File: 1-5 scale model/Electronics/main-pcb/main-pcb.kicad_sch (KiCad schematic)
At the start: 21 parts

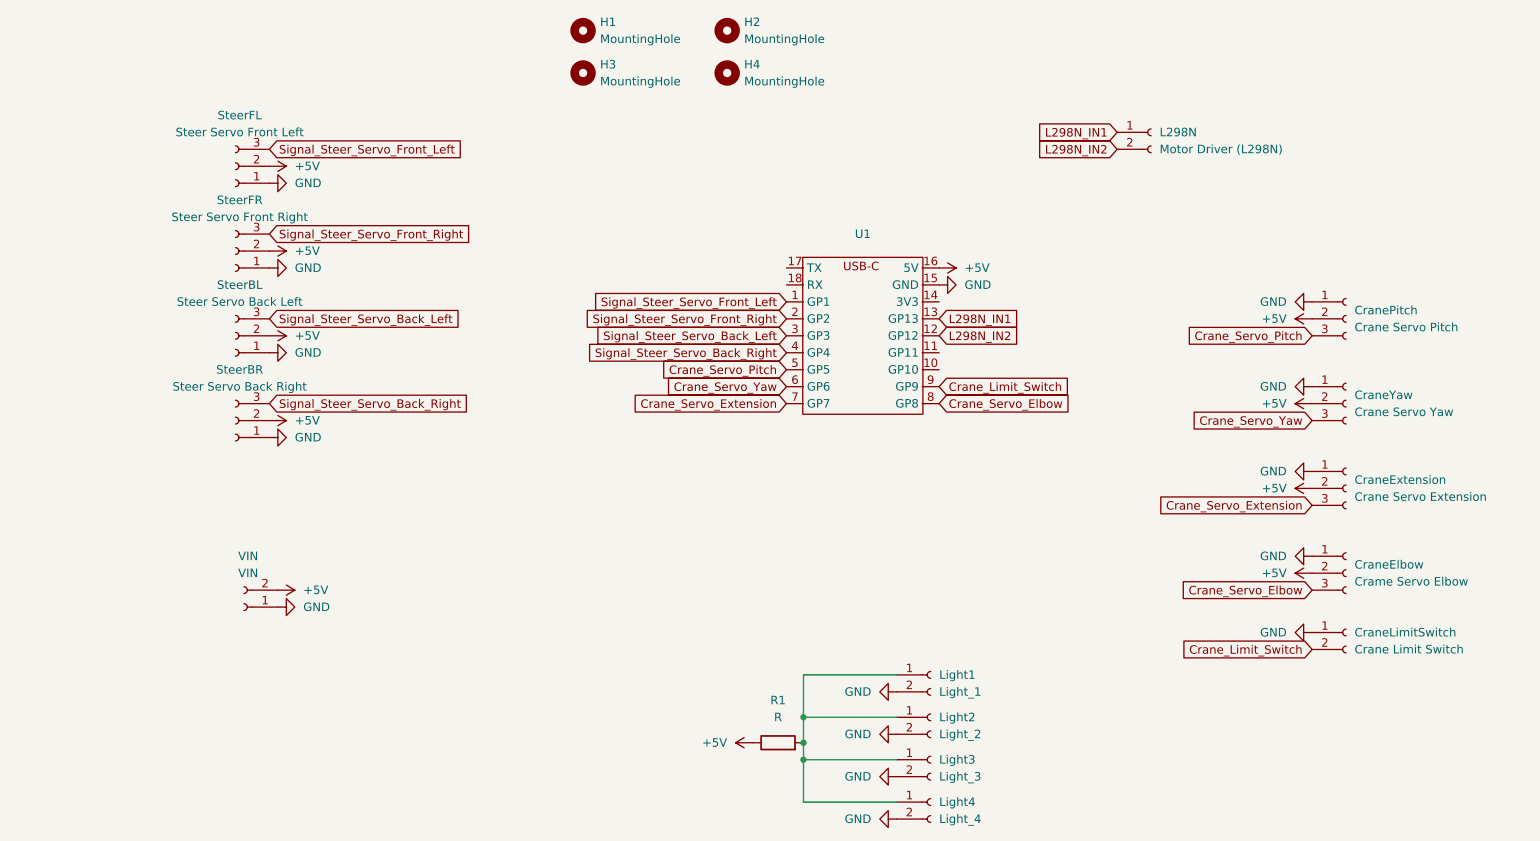
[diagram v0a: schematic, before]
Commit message: updated pitch motor
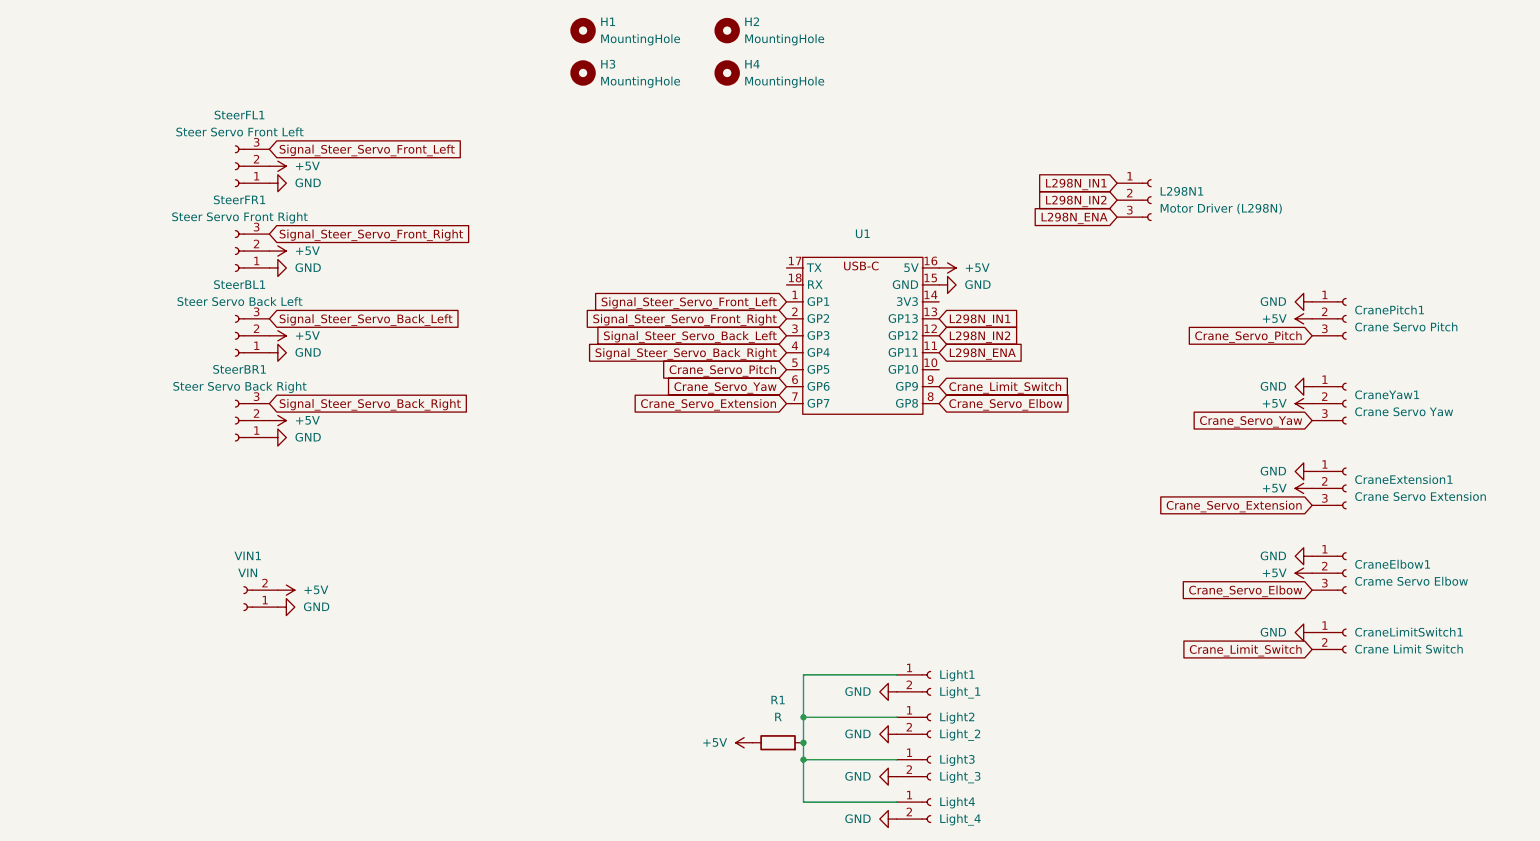
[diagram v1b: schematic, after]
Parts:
- removed L298N: Motor Driver (L298N), Connector_JST:JST_XH_B2B-XH-A_1x02_P2.50mm_Vertical, symbol Connector:Conn_01x02_Socket
- added L298N1: Motor Driver (L298N), Connector_JST:JST_XH_B3B-XH-A_1x03_P2.50mm_Vertical, symbol Connector:Conn_01x03_Socket
- renumbered CraneElbow to CraneElbow1, CraneExtension to CraneExtension1, CraneLimitSwitch to CraneLimitSwitch1, CranePitch to CranePitch1, CraneYaw to CraneYaw1, SteerBL to SteerBL1, SteerBR to SteerBR1, SteerFL to SteerFL1, SteerFR to SteerFR1, VIN to VIN1
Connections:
- net L298N_IN1: now also L298N1.1 (Pin_1)
- net L298N_IN2: now also L298N1.2 (Pin_2)
- net L298N_ENA: now reaches U1.11 (GP11)
- net L298N_ENA: now also L298N1.3 (Pin_3)
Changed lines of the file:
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@@
 		)
 	)
-	(global_label "L298N_IN1"
-		(shape input)
-		(at 195.58 53.34 180)
-		(fields_autoplaced yes)
-		(effects
-			(font
-				(size 1.27 1.27)
-			)
-			(justify right)
-		)
-		(property "Intersheetrefs" "${INTERSHEET_REFS}"
-			(at 182.4953 53.34 0)
-			(effects
-				(font
-					(size 1.27 1.27)
-				)
-				(justify right)
-				(hide yes)
-			)
-		)
-	)
 	(global_label "Signal_Steer_Servo_Back_Left"
 		(shape input)
@@
 		)
 	)
+	(global_label "L298N_IN2"
+		(shape input)
+		(at 195.58 63.5 180)
+		(fields_autoplaced yes)
+		(effects
+			(font
+				(size 1.27 1.27)
+			)
+			(justify right)
+		)
+		(property "Intersheetrefs" "${INTERSHEET_REFS}"
+			(at 182.4953 63.5 0)
+			(effects
+				(font
+					(size 1.27 1.27)
+				)
+				(justify right)
+				(hide yes)
+			)
+		)
+	)
 	(global_label "Signal_Steer_Servo_Back_Right"
 		(shape input)
@@
 		)
 	)
-	(global_label "L298N_IN2"
+	(global_label "Signal_Steer_Servo_Back_Left"
 		(shape input)
-		(at 195.58 55.88 180)
+		(at 68.58 81.28 0)
 		(fields_autoplaced yes)
 		(effects
@@
 				(size 1.27 1.27)
 			)
-			(justify right)
+			(justify left)
 		)
 		(property "Intersheetrefs" "${INTERSHEET_REFS}"
-			(at 182.4953 55.88 0)
+			(at 99.5654 81.28 0)
 			(effects
 				(font
 					(size 1.27 1.27)
 				)
-				(justify right)
+				(justify left)
 				(hide yes)
 			)
 		)
 	)
-	(global_label "Signal_Steer_Servo_Back_Left"
+	(global_label "Crane_Servo_Elbow"
 		(shape input)
-		(at 68.58 81.28 0)
+		(at 168.91 93.98 0)
 		(fields_autoplaced yes)
 		(effects
@@
 		)
 		(property "Intersheetrefs" "${INTERSHEET_REFS}"
-			(at 99.5654 81.28 0)
+			(at 189.9168 93.98 0)
 			(effects
 				(font
@@
 		)
 	)
-	(global_label "Crane_Servo_Elbow"
+	(global_label "Crane_Servo_Extension"
 		(shape input)
-		(at 168.91 93.98 0)
+		(at 146.05 93.98 180)
+		(fields_autoplaced yes)
+		(effects
+			(font
+				(size 1.27 1.27)
+			)
+			(justify right)
+		)
+		(property "Intersheetrefs" "${INTERSHEET_REFS}"
+			(at 121.4146 93.98 0)
+			(effects
+				(font
+					(size 1.27 1.27)
+				)
+				(justify right)
+				(hide yes)
+			)
+		)
+	)
+	(global_label "L298N_ENA"
+		(shape input)
+		(at 168.91 86.36 0)
 		(fields_autoplaced yes)
 		(effects
@@
 		)
 		(property "Intersheetrefs" "${INTERSHEET_REFS}"
-			(at 189.9168 93.98 0)
+			(at 182.418 86.36 0)
 			(effects
 				(font
@@
 		)
 	)
-	(global_label "Crane_Servo_Extension"
+	(global_label "L298N_IN1"
 		(shape input)
-		(at 146.05 93.98 180)
+		(at 195.58 60.96 180)
 		(fields_autoplaced yes)
 		(effects
@@
 		)
 		(property "Intersheetrefs" "${INTERSHEET_REFS}"
-			(at 121.4146 93.98 0)
+			(at 182.4953 60.96 0)
 			(effects
 				(font
@@
 		)
 	)
+	(global_label "L298N_ENA"
+		(shape input)
+		(at 195.58 66.04 180)
+		(fields_autoplaced yes)
+		(effects
+			(font
+				(size 1.27 1.27)
+			)
+			(justify right)
+		)
+		(property "Intersheetrefs" "${INTERSHEET_REFS}"
+			(at 182.072 66.04 0)
+			(effects
+				(font
+					(size 1.27 1.27)
+				)
+				(justify right)
+				(hide yes)
+			)
+		)
+	)
 	(symbol
 		(lib_id "power:+5V")
@@
 		(dnp no)
 		(fields_autoplaced yes)
-		(property "Reference" "CraneExtension"
+		(property "Reference" "CraneExtension1"
 			(at 231.14 105.4099 0)
 			(effects
@@
 			(project "main-pcb"
 				(path "/7ea8da9e-64ae-49f9-b37e-5eaa0e3ec503"
-					(reference "CraneExtension")
+					(reference "CraneExtension1")
 					(unit 1)
 				)
@@
 	)
 	(symbol
+		(lib_id "Connector:Conn_01x03_Socket")
+		(at 200.66 63.5 0)
+		(unit 1)
+		(exclude_from_sim no)
+		(in_bom yes)
+		(on_board yes)
+		(dnp no)
+		(fields_autoplaced yes)
+		(property "Reference" "L298N1"
+			(at 201.93 62.2299 0)
+			(effects
+				(font
+					(size 1.27 1.27)
+				)
+				(justify left)
+			)
+		)
+		(property "Value" "Motor Driver (L298N)"
+			(at 201.93 64.7699 0)
+			(effects
+				(font
+					(size 1.27 1.27)
+				)
+				(justify left)
+			)
+		)
+		(property "Footprint" "Connector_JST:JST_XH_B3B-XH-A_1x03_P2.50mm_Vertical"
+			(at 200.66 63.5 0)
+			(effects
+				(font
+					(size 1.27 1.27)
+				)
+				(hide yes)
+			)
+		)
+		(property "Datasheet" "~"
+			(at 200.66 63.5 0)
+			(effects
+				(font
+					(size 1.27 1.27)
+				)
+				(hide yes)
+			)
+		)
+		(property "Description" "Generic connector, single row, 01x03, script generated"
+			(at 200.66 63.5 0)
+			(effects
+				(font
+					(size 1.27 1.27)
+				)
+				(hide yes)
+			)
+		)
+		(pin "2"
+		)
+		(pin "1"
+		)
+		(pin "3"
+		)
+		(instances
+			(project "main-pcb"
+				(path "/7ea8da9e-64ae-49f9-b37e-5eaa0e3ec503"
+					(reference "L298N1")
+					(unit 1)
+				)
+			)
+		)
+	)
+	(symbol
 		(lib_id "Connector:Conn_01x02_Socket")
 		(at 64.77 124.46 180)
@@
 		(dnp no)
 		(fields_autoplaced yes)
-		(property "Reference" "VIN"
+		(property "Reference" "VIN1"
 			(at 65.405 116.84 0)
 			(effects
@@
 			(project "main-pcb"
 				(path "/7ea8da9e-64ae-49f9-b37e-5eaa0e3ec503"
-					(reference "VIN")
+					(reference "VIN1")
 					(unit 1)
 				)
@@
 		(dnp no)
 		(fields_autoplaced yes)
-		(property "Reference" "SteerBL"
+		(property "Reference" "SteerBL1"
 			(at 64.135 76.2 0)
 			(effects
@@
 			(project "main-pcb"
 				(path "/7ea8da9e-64ae-49f9-b37e-5eaa0e3ec503"
-					(reference "SteerBL")
+					(reference "SteerBL1")
 					(unit 1)
 				)
@@
 		(dnp no)
 		(fields_autoplaced yes)
-		(property "Reference" "SteerFR"
+		(property "Reference" "SteerFR1"
 			(at 64.135 63.5 0)
 			(effects
@@
 			(project "main-pcb"
 				(path "/7ea8da9e-64ae-49f9-b37e-5eaa0e3ec503"
-					(reference "SteerFR")
-					(unit 1)
-				)
-			)
-		)
-	)
-	(symbol
-		(lib_id "Connector:Conn_01x02_Socket")
-		(at 200.66 53.34 0)
-		(unit 1)
-		(exclude_from_sim no)
-		(in_bom yes)
-		(on_board yes)
-		(dnp no)
-		(fields_autoplaced yes)
-		(property "Reference" "L298N"
-			(at 201.93 53.3399 0)
-			(effects
-				(font
-					(size 1.27 1.27)
-				)
-				(justify left)
-			)
-		)
-		(property "Value" "Motor Driver (L298N)"
-			(at 201.93 55.8799 0)
-			(effects
-				(font
-					(size 1.27 1.27)
-				)
-				(justify left)
-			)
-		)
-		(property "Footprint" "Connector_JST:JST_XH_B2B-XH-A_1x02_P2.50mm_Vertical"
-			(at 200.66 53.34 0)
-			(effects
-				(font
-					(size 1.27 1.27)
-				)
-				(hide yes)
-			)
-		)
-		(property "Datasheet" "~"
-			(at 200.66 53.34 0)
-			(effects
-				(font
-					(size 1.27 1.27)
-				)
-				(hide yes)
-			)
-		)
-		(property "Description" "Generic connector, single row, 01x02, script generated"
-			(at 200.66 53.34 0)
-			(effects
-				(font
-					(size 1.27 1.27)
-				)
-				(hide yes)
-			)
-		)
-		(pin "1"
-		)
-		(pin "2"
-		)
-		(instances
-			(project "main-pcb"
-				(path "/7ea8da9e-64ae-49f9-b37e-5eaa0e3ec503"
-					(reference "L298N")
+					(reference "SteerFR1")
 					(unit 1)
 				)
@@
 		(dnp no)
 		(fields_autoplaced yes)
-		(property "Reference" "SteerBR"
+		(property "Reference" "SteerBR1"
 			(at 64.135 88.9 0)
 			(effects
@@
 			(project "main-pcb"
 				(path "/7ea8da9e-64ae-49f9-b37e-5eaa0e3ec503"
-					(reference "SteerBR")
+					(reference "SteerBR1")
 					(unit 1)
 				)
@@
 		(dnp no)
 		(fields_autoplaced yes)
-		(property "Reference" "CraneLimitSwitch"
+		(property "Reference" "CraneLimitSwitch1"
 			(at 231.14 128.2699 0)
 			(effects
@@
 			(project ""
 				(path "/7ea8da9e-64ae-49f9-b37e-5eaa0e3ec503"
-					(reference "CraneLimitSwitch")
+					(reference "CraneLimitSwitch1")
 					(unit 1)
 				)
@@
 		(dnp no)
 		(fields_autoplaced yes)
-		(property "Reference" "CraneElbow"
+		(property "Reference" "CraneElbow1"
 			(at 231.14 118.1099 0)
 			(effects
@@
 			(project "main-pcb"
 				(path "/7ea8da9e-64ae-49f9-b37e-5eaa0e3ec503"
-					(reference "CraneElbow")
+					(reference "CraneElbow1")
 					(unit 1)
 				)
@@
 		(dnp no)
 		(fields_autoplaced yes)
-		(property "Reference" "SteerFL"
+		(property "Reference" "SteerFL1"
 			(at 64.135 50.8 0)
 			(effects
@@
 			(project "main-pcb"
 				(path "/7ea8da9e-64ae-49f9-b37e-5eaa0e3ec503"
-					(reference "SteerFL")
+					(reference "SteerFL1")
 					(unit 1)
 				)
@@
 		(dnp no)
 		(fields_autoplaced yes)
-		(property "Reference" "CraneYaw"
+		(property "Reference" "CraneYaw1"
 			(at 231.14 92.7099 0)
 			(effects
@@
 			(project "main-pcb"
 				(path "/7ea8da9e-64ae-49f9-b37e-5eaa0e3ec503"
-					(reference "CraneYaw")
+					(reference "CraneYaw1")
 					(unit 1)
 				)
@@
 		(dnp no)
 		(fields_autoplaced yes)
-		(property "Reference" "CranePitch"
+		(property "Reference" "CranePitch1"
 			(at 231.14 80.0099 0)
 			(effects
@@
 			(project "main-pcb"
 				(path "/7ea8da9e-64ae-49f9-b37e-5eaa0e3ec503"
-					(reference "CranePitch")
+					(reference "CranePitch1")
 					(unit 1)
 				)

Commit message: added battery voltage detector
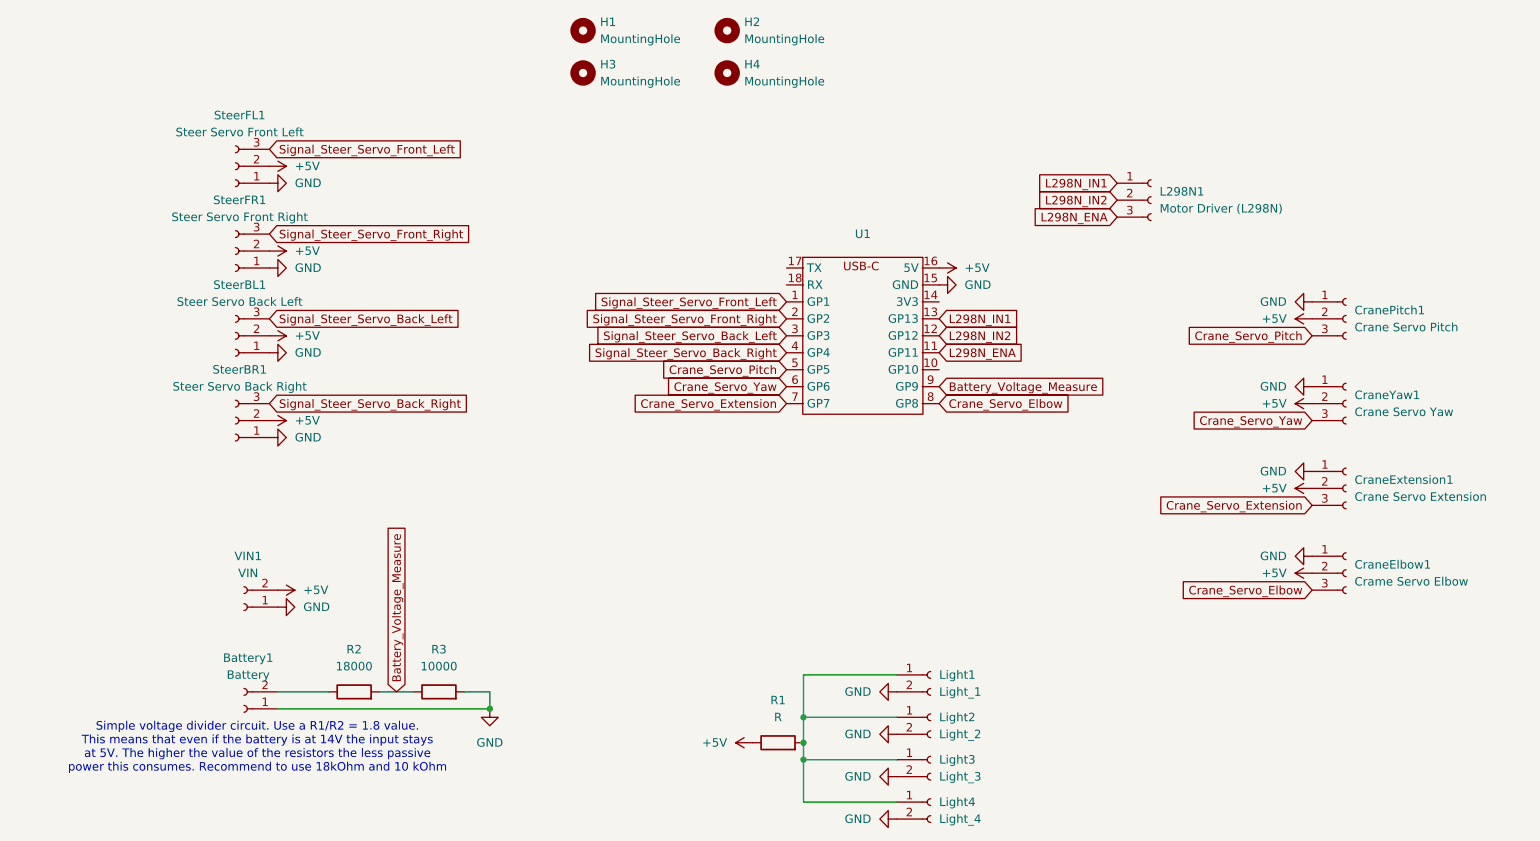
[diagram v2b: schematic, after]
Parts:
- removed CraneLimitSwitch1: Crane Limit Switch, Connector_JST:JST_XH_B2B-XH-A_1x02_P2.50mm_Vertical, symbol Connector:Conn_01x02_Socket
- added Battery1: Battery, Connector_JST:JST_XH_B2B-XH-A_1x02_P2.50mm_Vertical, symbol Connector:Conn_01x02_Socket
- added R2: 18000, Resistor_THT:R_Axial_DIN0207_L6.3mm_D2.5mm_P10.16mm_Horizontal, symbol Device:R
- added R3: 10000, Resistor_THT:R_Axial_DIN0207_L6.3mm_D2.5mm_P10.16mm_Horizontal, symbol Device:R
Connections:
- net GND: now also Battery1.1 (Pin_1), R3.2
- net Crane_Limit_Switch renamed Battery_Voltage_Measure
- net Battery_Voltage_Measure: now also R2.2, R3.1
- new net: Battery1.2 (Pin_2), R2.1
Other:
- note added: "Simple voltage divider circuit. Use a R1/R2 = 1.8 value. This means that even if the battery is at 14V the input stays at 5V. The higher the value of the resistors the less passive power this consumes. Recommend to use 18kOhm and 10 kOhm"
